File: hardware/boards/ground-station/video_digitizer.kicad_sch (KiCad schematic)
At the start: 34 parts, among them U601 ADV7282A-M, U602 AP2127K-1.8, U603 AP2127K-1.8, Y601 28.63636 MHz

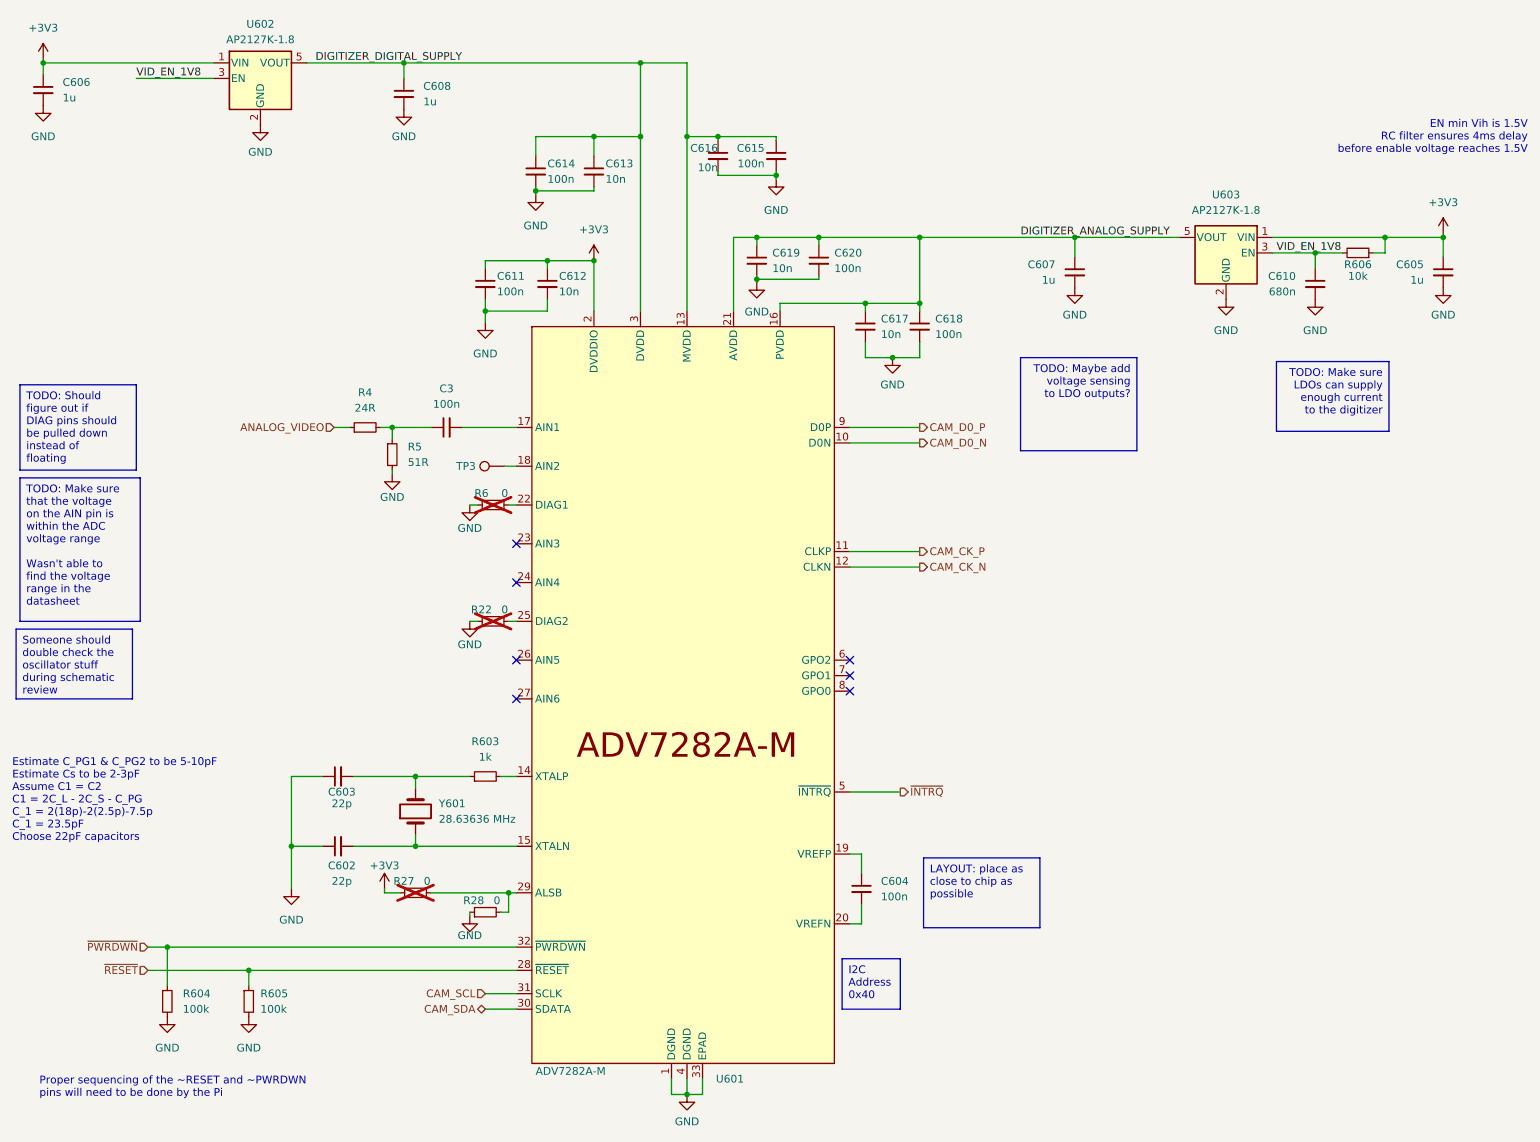
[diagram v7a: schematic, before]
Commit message: Did initial layout. Still need to connect everything together
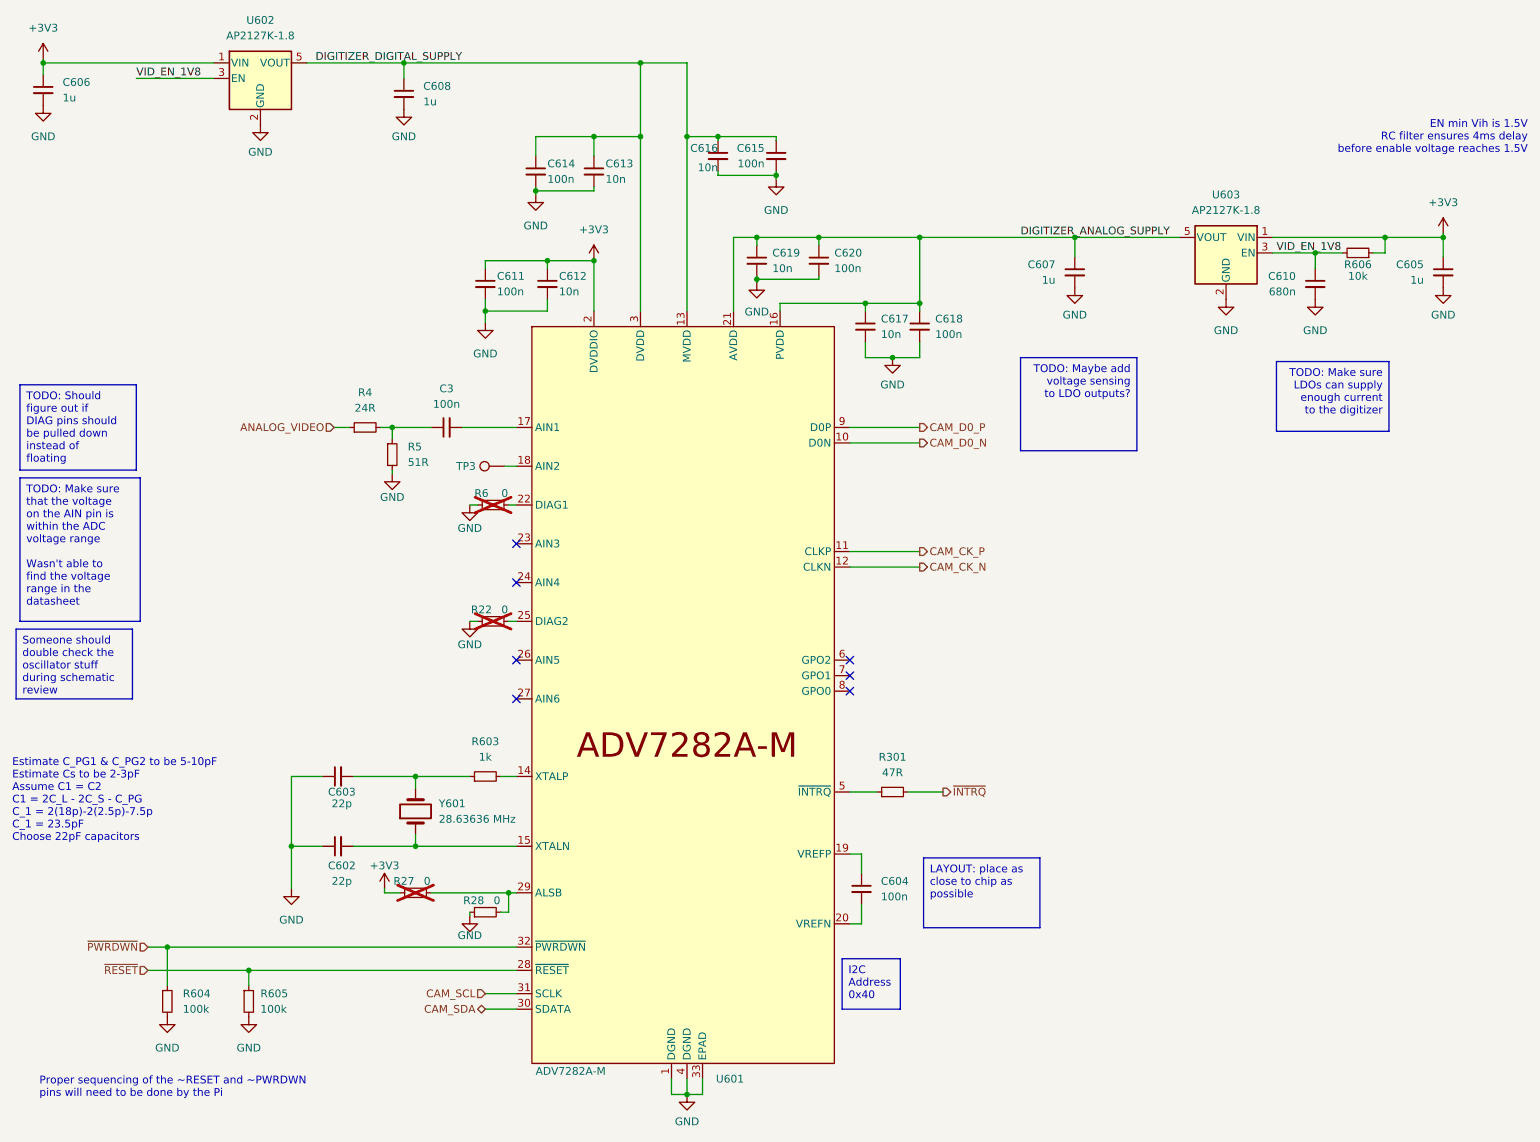
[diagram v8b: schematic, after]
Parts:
- added R301: 47R, Resistor_SMD:R_0201_0603Metric, symbol Device:R_Small
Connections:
- net ~{INTRQ}: now also R301.2; no longer U601.5 (~{INTRQ})
- new net: R301.1, U601.5 (~{INTRQ})
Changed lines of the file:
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@@
+    (stroke (width 0) (type default))
+  )
+  (wire (pts (xy 161.925 139.065) (xy 167.64 139.065))
     (stroke (width 0) (type default))
   )
@@
     (stroke (width 0) (type default))
   )
+  (wire (pts (xy 156.845 139.065) (xy 152.4 139.065))
+    (stroke (width 0) (type default))
+  )
   (wire (pts (xy 71.12 147.955) (xy 81.28 147.955))
     (stroke (width 0) (type default))
@@
   )
   (wire (pts (xy 221.615 50.8) (xy 228.6 50.8))
-    (stroke (width 0) (type default))
-  )
-  (wire (pts (xy 160.655 139.065) (xy 152.4 139.065))
     (stroke (width 0) (type default))
   )
@@
     (effects (font (size 1.27 1.27)) (justify right))
   )
-  (hierarchical_label "~{INTRQ}" (shape output) (at 160.655 139.065 0) (fields_autoplaced)
+  (hierarchical_label "~{INTRQ}" (shape output) (at 167.64 139.065 0) (fields_autoplaced)
     (effects (font (size 1.27 1.27)) (justify left))
   )
@@
         (path "/ce329892-de08-4d39-b253-15f3aaf1c085/00cfc561-e5dc-4c70-afbd-7533b8052400"
           (reference "R603") (unit 1)
+        )
+      )
+    )
+  )
+  (symbol (lib_id "Device:R_Small") (at 159.385 139.065 90) (unit 1)
+    (in_bom yes) (on_board yes) (dnp no) (fields_autoplaced)
+    (property "Reference" "R301" (at 159.385 133.35 90)
+      (effects (font (size 1.27 1.27)))
+    )
+    (property "Value" "47R" (at 159.385 135.89 90)
+      (effects (font (size 1.27 1.27)))
+    )
+    (property "Footprint" "Resistor_SMD:R_0201_0603Metric" (at 159.385 139.065 0)
+      (effects (font (size 1.27 1.27)) hide)
+    )
+    (property "Datasheet" "~" (at 159.385 139.065 0)
+      (effects (font (size 1.27 1.27)) hide)
+    )
+    (pin "1")
+    (pin "2")
+    (instances
+      (project "ground-station"
+        (path "/ce329892-de08-4d39-b253-15f3aaf1c085/00cfc561-e5dc-4c70-afbd-7533b8052400"
+          (reference "R301") (unit 1)
         )
       )
@@
   (symbol (lib_id "Regulator_Linear:AP2127K-1.8") (at 55.88 22.225 0) (unit 1)
     (in_bom yes) (on_board yes) (dnp no) (fields_autoplaced)
-    (property "Reference" "U602" (at 55.88 13.335 0)
-      (effects (font (size 1.27 1.27)))
-    )
-    (property "Value" "AP2127K-1.8" (at 55.88 15.875 0)
-      (effects (font (size 1.27 1.27)))
-    )
+    (property "Reference" "U602" (at 55.88 12.7 0)
+      (effects (font (size 1.27 1.27)))
+    )
+    (property "Value" "AP2127K-1.8" (at 55.88 15.24 0)
+      (effects (font (size 1.27 1.27)))
+    )
